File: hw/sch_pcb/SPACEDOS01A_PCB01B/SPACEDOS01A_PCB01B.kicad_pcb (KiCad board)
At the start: 2 copper layers, 90.9 x 50.3 mm, 111 parts, among them J1 HEADER_2x01_PARALLEL, J19 HEADER_2x01_PARALLEL, J2 HEADER_2x01_PARALLEL, J22 HEADER_2x03, J3 HEADER_2x01_PARALLEL, J4 HEADER_1x01, J5 HEADER_1x01, J6 HEADER_1x01, J7 HEADER_1x01, M1 HOLE, M2 HOLE, M3 HOLE, M4 HOLE, M5 BMI-S-210-F, M6 BMI-S-210-F, M7 BMI-S-210-F, M8 BMI-S-204-F, U1 OPA2314, U10 ATMEGA1284P-AU, U11 PCF85263A, U2 OPA2314, U3 ISL21080DIH312Z-TK 1V25, U4 TS7211, U5 TS5A4594, U6 TPS613221ADBV, U8 TPS613222ADBV, Y1 16MHz, Y2 ABS07-120-32.768KHZ-T

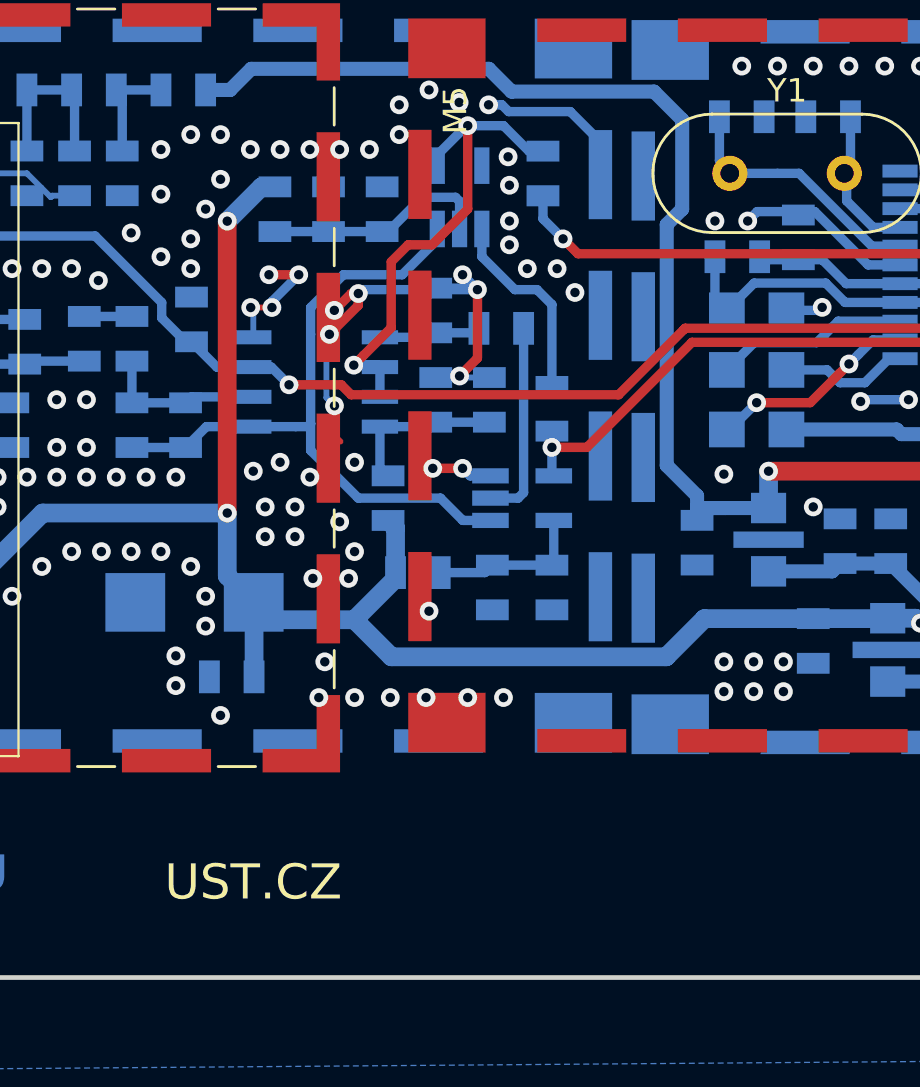
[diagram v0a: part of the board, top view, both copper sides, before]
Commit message: Editace PCB a generování vyrobních dat.
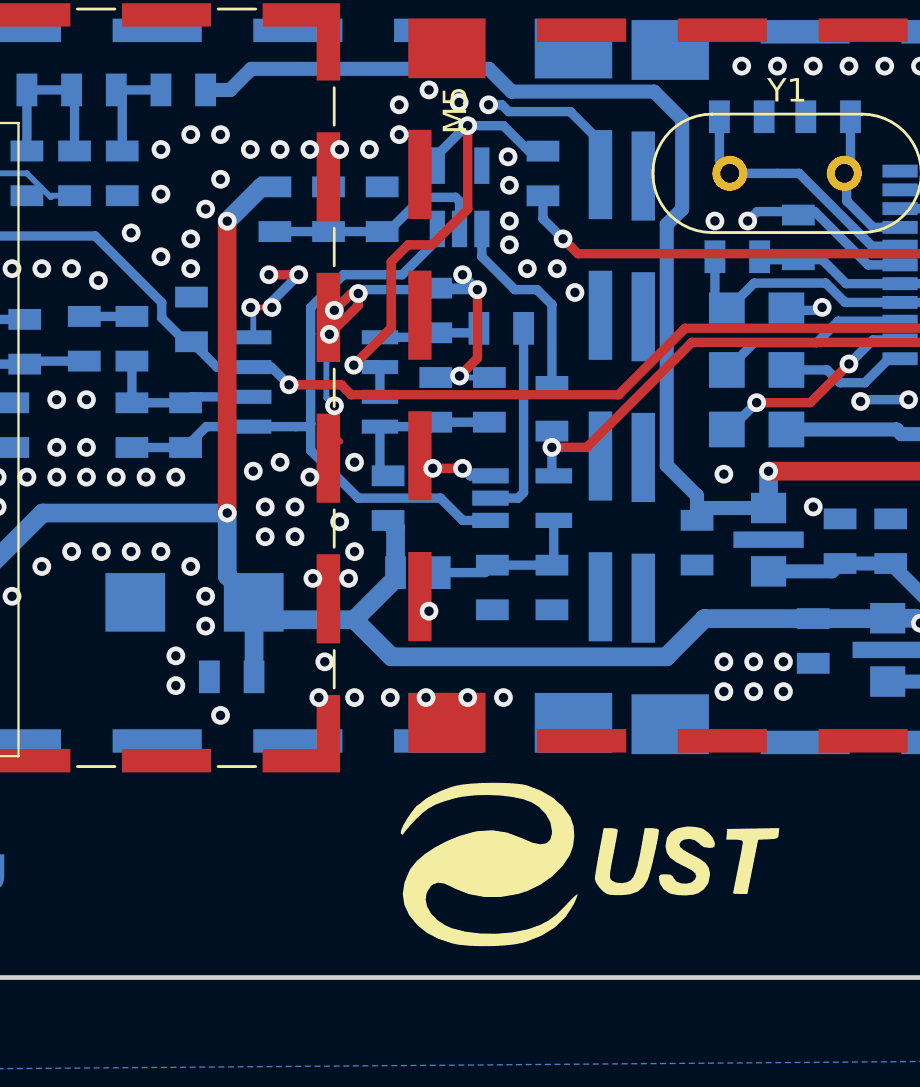
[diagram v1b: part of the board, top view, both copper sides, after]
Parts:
- added G***: LOGO, MLAB_LOGA:UST, F.Cu at (44.3, -5.08)
- C29, C45, C51, C52: footprint Mlab_L:FIR1 -> Mlab_L:FIR_0805
